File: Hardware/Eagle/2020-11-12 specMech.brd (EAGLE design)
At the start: 142.2 x 121.9 mm, 86 parts, among them J1 PINHD-1X8-MOLEX-SHROUD, J2 JST-2-PIN-2B-PH-K-S(LF)(SN), J3 PINHD-1X8-MOLEX-SHROUD, J4 PINHD-1X8-MOLEX-SHROUD, J6 Molex 0022232081, J7 Lantronix XPORT, J8 Molex 0022232081, U1 MCP23008-E/SO, U10 ADS1115, U11 MCP23008-E/SO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

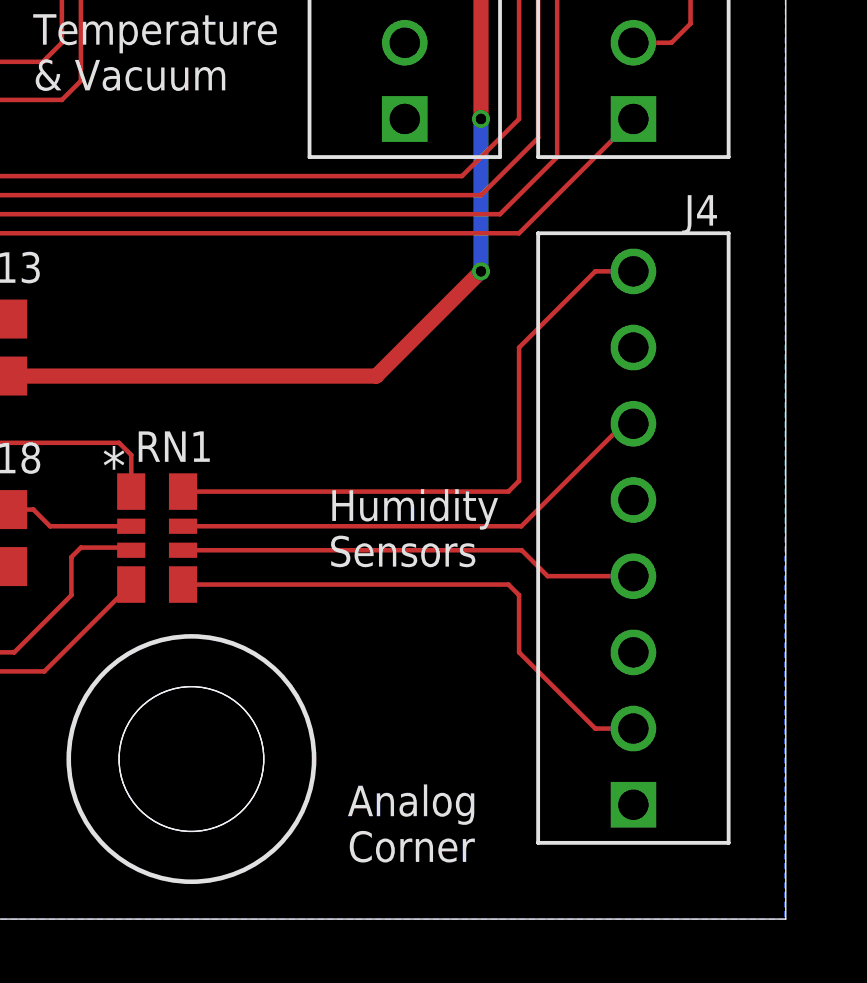
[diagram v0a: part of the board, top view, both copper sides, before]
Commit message: Added fan control
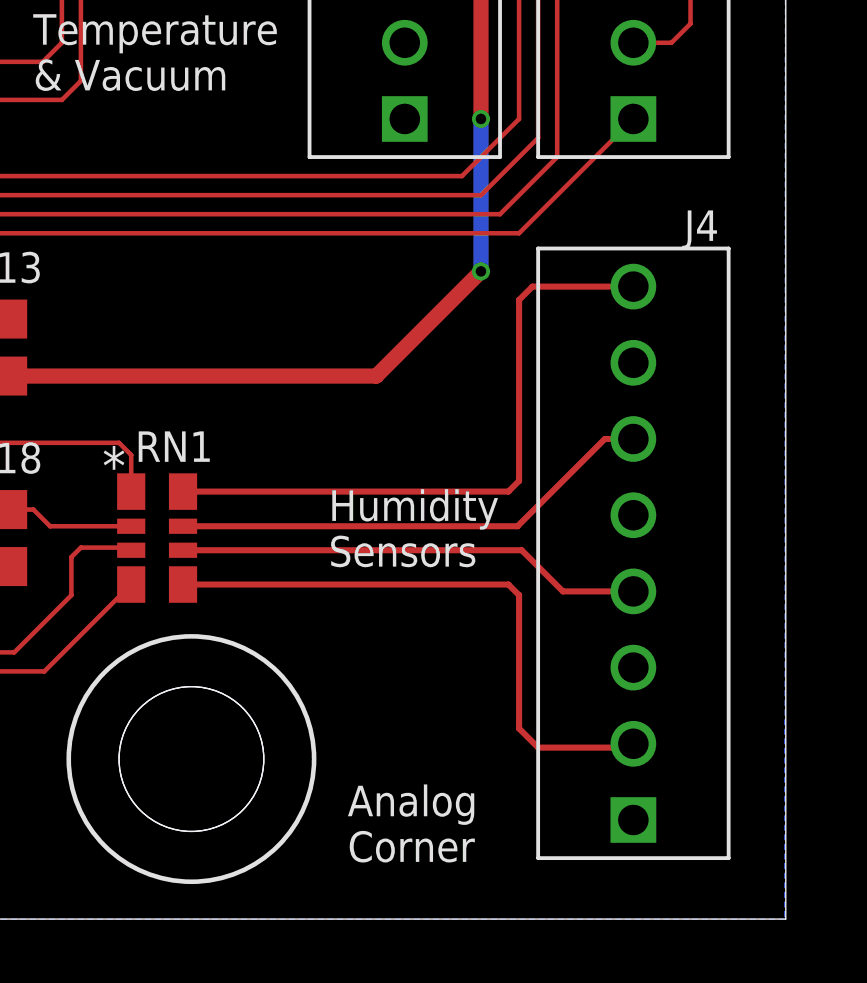
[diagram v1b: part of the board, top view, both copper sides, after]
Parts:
- moved J4 0.51 mm to (137.2, 12.2)
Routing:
- net A0B: track 18.1 -> 19.9 mm
- net A3B: track 20.7 -> 21.4 mm
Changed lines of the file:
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@@
 <drawing>
 <settings>
-<setting alwaysvectorfont="no"/>
+<setting alwaysvectorfont="yes"/>
 <setting verticaltext="up"/>
 </settings>
@@
 </autorouter>
 <elements>
-<element name="J4" library="AUmlib" library_urn="urn:adsk.eagle:library:9166017" package="1X08-MOLEX-SHROUD" package3d_urn="urn:adsk.eagle:package:18132194/5" value="PINHD-1X8-MOLEX-SHROUD" x="137.16" y="12.7" smashed="yes" rot="R180">
-<attribute name="NAME" x="140.0175" y="24.13" size="1.016" layer="25" font="vector" rot="R180"/>
+<element name="J4" library="AUmlib" library_urn="urn:adsk.eagle:library:9166017" package="1X08-MOLEX-SHROUD" package3d_urn="urn:adsk.eagle:package:18132194/5" value="PINHD-1X8-MOLEX-SHROUD" x="137.16" y="12.192" smashed="yes" rot="R180">
+<attribute name="NAME" x="140.0175" y="23.622" size="1.016" layer="25" font="vector" rot="R180"/>
 </element>
 <element name="J6" library="AUmlib" library_urn="urn:adsk.eagle:library:9166017" package="1X08-MOLEX-SHROUD" package3d_urn="urn:adsk.eagle:package:18132194/5" value="Molex 0022232081" x="137.16" y="88.392" smashed="yes" rot="R180">
@@
 <contactref element="RN1" pad="5"/>
 <contactref element="J4" pad="P$2"/>
-<wire x1="122.1486" y1="11.1506" x2="132.9944" y2="11.1506" width="0.1524" layer="1"/>
-<wire x1="132.9944" y1="11.1506" x2="133.35" y2="10.795" width="0.1524" layer="1"/>
-<wire x1="133.35" y1="10.795" x2="133.35" y2="8.89" width="0.1524" layer="1"/>
-<wire x1="133.35" y1="8.89" x2="135.89" y2="6.35" width="0.1524" layer="1"/>
-<wire x1="135.89" y1="6.35" x2="137.16" y2="6.35" width="0.1524" layer="1"/>
+<wire x1="122.1486" y1="11.1506" x2="132.9944" y2="11.1506" width="0.2032" layer="1"/>
+<wire x1="133.35" y1="10.795" x2="132.9944" y2="11.1506" width="0.2032" layer="1"/>
+<wire x1="137.16" y1="5.842" x2="137.033" y2="5.715" width="0.2032" layer="1"/>
+<wire x1="133.985" y1="5.715" x2="133.35" y2="6.35" width="0.2032" layer="1"/>
+<wire x1="137.033" y1="5.715" x2="133.985" y2="5.715" width="0.2032" layer="1"/>
+<wire x1="133.35" y1="6.35" x2="133.35" y2="10.795" width="0.2032" layer="1"/>
 </signal>
 <signal name="A1B">
 <contactref element="RN1" pad="6"/>
 <contactref element="J4" pad="P$4"/>
-<wire x1="122.1486" y1="12.2938" x2="133.4387" y2="12.2938" width="0.1524" layer="1"/>
-<wire x1="134.3025" y1="11.43" x2="137.16" y2="11.43" width="0.1524" layer="1"/>
-<wire x1="133.4387" y1="12.2938" x2="134.3025" y2="11.43" width="0.1524" layer="1"/>
+<wire x1="122.1486" y1="12.2938" x2="133.4387" y2="12.2938" width="0.2032" layer="1"/>
+<wire x1="137.16" y1="10.922" x2="134.8105" y2="10.922" width="0.2032" layer="1"/>
+<wire x1="134.8105" y1="10.922" x2="133.4387" y2="12.2938" width="0.2032" layer="1"/>
 </signal>
 <signal name="A2B">
 <contactref element="RN1" pad="7"/>
 <contactref element="J4" pad="P$6"/>
-<wire x1="122.1486" y1="13.0938" x2="133.4263" y2="13.0938" width="0.1524" layer="1"/>
-<wire x1="136.8425" y1="16.51" x2="137.16" y2="16.51" width="0.1524" layer="1"/>
-<wire x1="133.4263" y1="13.0938" x2="136.8425" y2="16.51" width="0.1524" layer="1"/>
+<wire x1="122.1486" y1="13.0938" x2="133.2993" y2="13.0938" width="0.2032" layer="1"/>
+<wire x1="136.2075" y1="16.002" x2="133.2993" y2="13.0938" width="0.2032" layer="1"/>
+<wire x1="136.2075" y1="16.002" x2="137.16" y2="16.002" width="0.2032" layer="1"/>
 </signal>
 <signal name="A3B">
 <contactref element="RN1" pad="8"/>
 <contactref element="J4" pad="P$8"/>
-<wire x1="122.1486" y1="14.2494" x2="132.9944" y2="14.2494" width="0.1524" layer="1"/>
-<wire x1="132.9944" y1="14.2494" x2="133.35" y2="14.605" width="0.1524" layer="1"/>
-<wire x1="133.35" y1="14.605" x2="133.35" y2="19.05" width="0.1524" layer="1"/>
-<wire x1="133.35" y1="19.05" x2="135.89" y2="21.59" width="0.1524" layer="1"/>
-<wire x1="135.89" y1="21.59" x2="137.16" y2="21.59" width="0.1524" layer="1"/>
+<wire x1="122.1486" y1="14.2494" x2="132.9944" y2="14.2494" width="0.2032" layer="1"/>
+<wire x1="132.9944" y1="14.2494" x2="133.35" y2="14.605" width="0.2032" layer="1"/>
+<wire x1="133.35" y1="14.605" x2="133.35" y2="20.6375" width="0.2032" layer="1"/>
+<wire x1="133.35" y1="20.6375" x2="133.7945" y2="21.082" width="0.2032" layer="1"/>
+<wire x1="133.7945" y1="21.082" x2="137.16" y2="21.082" width="0.2032" layer="1"/>
 </signal>
 <signal name="N$5">

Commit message: Forced rebootack to be !<CR> EXACTLY
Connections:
- net RC-RX: now also CNANO1.PC1-RX, U12.4; no longer CNANO1.PC0-TX, U12.1
- net RC-TX: now also CNANO1.PC0-TX, U12.1; no longer CNANO1.PC1-RX, U12.4
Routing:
- net RC-TX: track 37.2 -> 40.5 mm
- net RC-RX: track 40.5 -> 37.2 mm
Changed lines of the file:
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@@
 <attribute name="NAME" x="117.1575" y="90.4875" size="1.016" layer="25" font="vector"/>
 <attribute name="POPULARITY" value="35" x="127" y="83.82" size="1.778" layer="27" rot="R270" display="off"/>
-<attribute name="VALUE" x="113.665" y="90.17" size="1.016" layer="27" font="vector" rot="R270"/>
 </element>
 <element name="U12" library="AUmlib" library_urn="urn:adsk.eagle:library:9166017" package="SOP95P275X110-6" package3d_urn="urn:adsk.eagle:package:9152015/2" value="74HC2G17TSSOP-6" x="107.315" y="84.455" smashed="yes">
@@
 <wire x1="115.89" y1="18.415" x2="116.205" y2="18.1" width="0.254" layer="1"/>
 </signal>
-<signal name="RC-TX">
+<signal name="RC-RX">
 <contactref element="CNANO1" pad="PC1-RX"/>
 <contactref element="U12" pad="4"/>
@@
 <wire x1="108.585" y1="83.4792" x2="108.5592" y2="83.505" width="0.1524" layer="1"/>
 </signal>
-<signal name="RC-RX">
+<signal name="RC-TX">
 <contactref element="CNANO1" pad="PC0-TX"/>
 <contactref element="U12" pad="1"/>
